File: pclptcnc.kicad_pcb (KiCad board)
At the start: 2 copper layers, 180.5 x 52.3 mm, 249 parts, among them P1 ARK825A-3, P3 ARK825A-4, P4 ARK825A-3, P5 ARK825A-3, P6 ARK825A-3, P7 ARK825A-3, P8 ARK825A-3, Q1 BC807-40, Q10 BC807-40, Q11 BC807-40, Q12 BC807-40, Q13 BC807-40, Q14 BC807-40, Q15 BC807-40, Q16 BC807-40, Q17 BC807-40, Q18 BC807-40, Q2 BC807-40, Q3 BC807-40, Q4 BC807-40, Q5 BC807-40, Q6 BC807-40, Q7 BC807-40, Q8 BC807-40, Q9 BC807-40, U1 74LVC1G3157GW, U10 SN74LVC2G17, U11 74HCT14, U12 SN74LVC2G17, U13 74HCT14, U2 HCPL2630, U3 HCPL2630, U4 HCPL2630, U5 HCPL2630, U6 HCPL2630, U7 HCPL2630, U8 74HCT14, U9 74HCT14, j1 DB25, j2 DB25

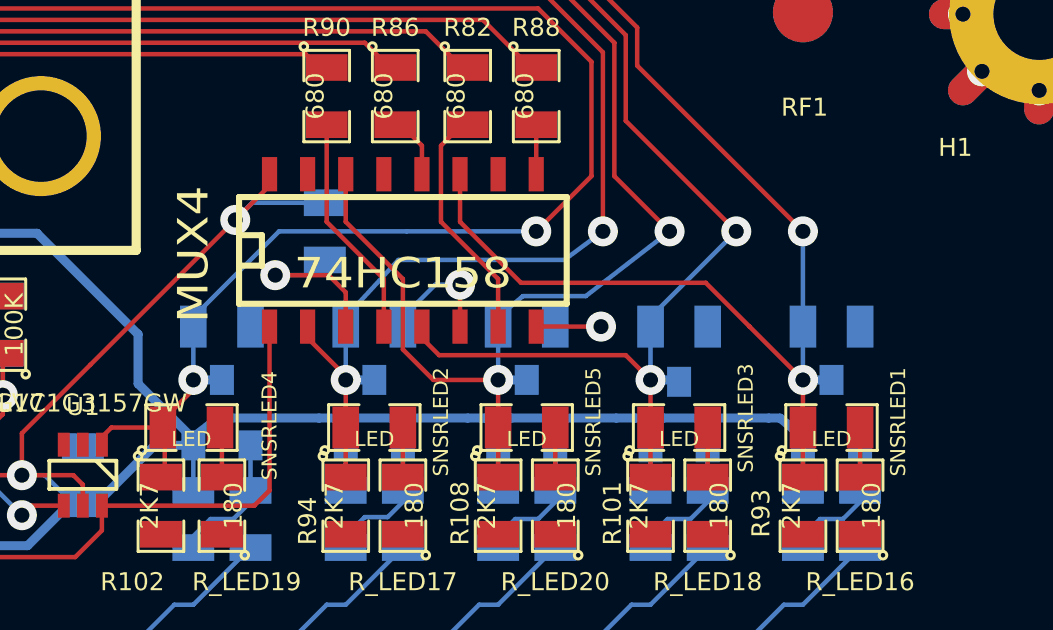
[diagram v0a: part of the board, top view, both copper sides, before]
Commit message: odd komponents removed
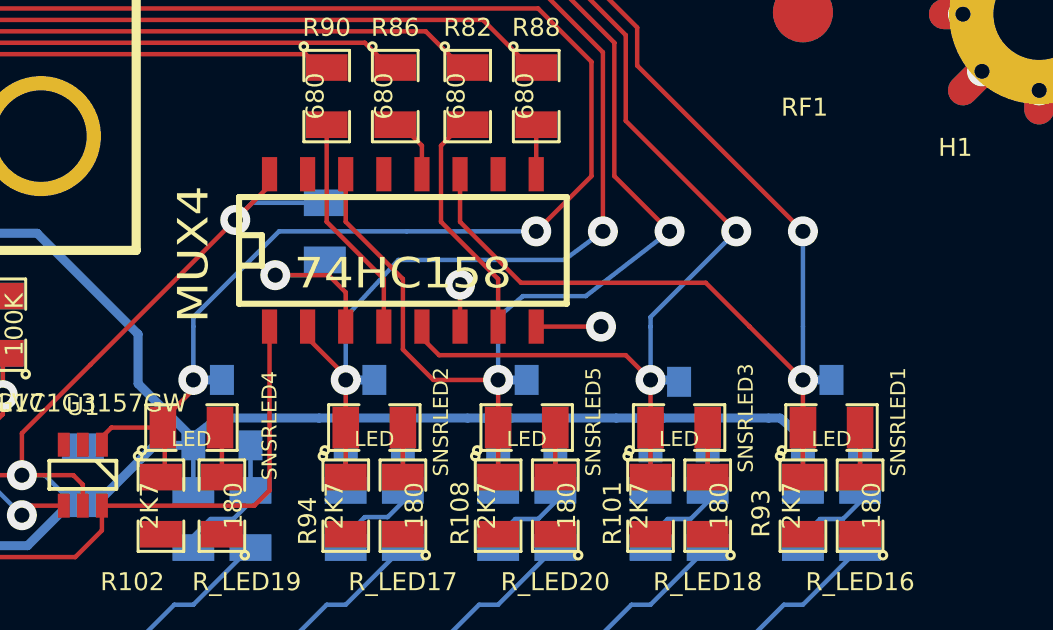
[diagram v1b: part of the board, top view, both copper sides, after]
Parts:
- removed R111, R112, R113, R114, R115: 100K, SM0805
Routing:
- net GND: track 391.3 -> 388.7 mm

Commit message: revision b
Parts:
- moved OPTOCPLR1 49.6 mm to (231.1, 108.6)
- moved OPTOCPLR5 49.6 mm to (220.9, 108.6)
- moved Q18 49.6 mm to (225.0, 92.1)
- moved R103 49.6 mm to (229.2, 95.6)
- moved R105 49.6 mm to (231.1, 95.6)
- moved R107 49.6 mm to (220.9, 111.2)
- moved R76 49.6 mm to (185.0, 117.5)
- moved R91 49.6 mm to (231.1, 111.2)
- moved R96 49.6 mm to (219.0, 95.6)
- moved R98 49.6 mm to (220.9, 95.6)
- moved SNSRLED5 49.6 mm to (225.0, 92.6)
- moved U12 49.6 mm to (206.2, 94.2)
- moved j2 49.6 mm to (185.4, 84.1)
- moved C5 49.6 mm to (95.7, 87.6)
- moved MUX4 49.6 mm to (220.9, 86.7)
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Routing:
- net /ISOLATED_GND: track 24.8 -> 55.5 mm, vias 1 -> 2
- net GND: track 388.7 -> 398.3 mm
- net /VCC_NFused: track 0.00 -> 3.41 mm
- net /ISOLATED_VCC: track 626.3 -> 629.4 mm
- net (no net): vias 1 -> 0
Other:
- board text added: "GND"
- board text added: "VCC"
- board text added: "VIN"

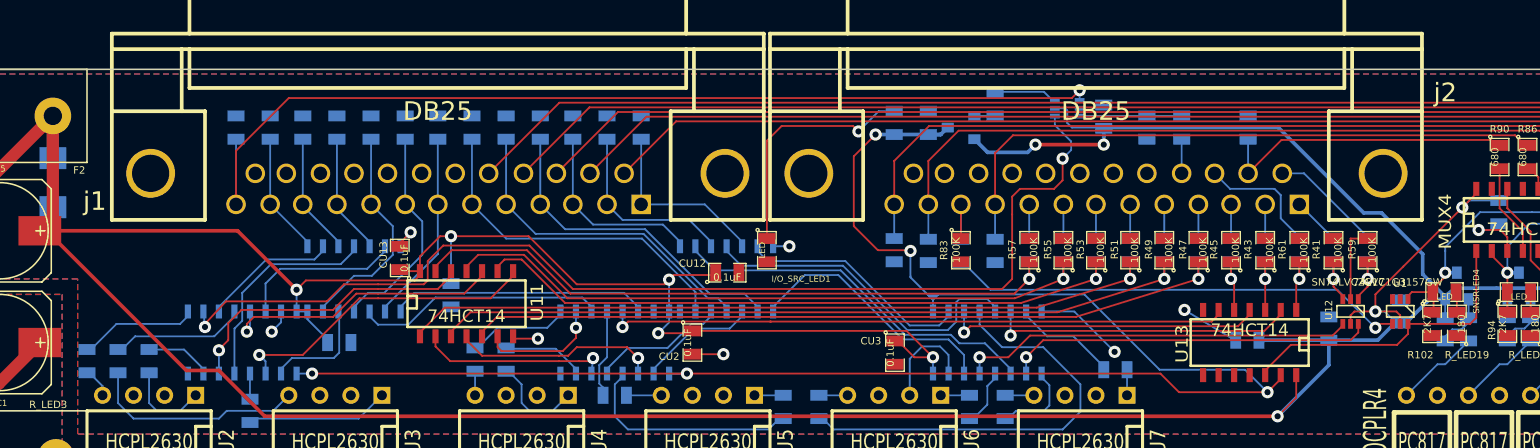
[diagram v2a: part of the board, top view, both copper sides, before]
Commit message: starting work on adding emergency stop switch selection
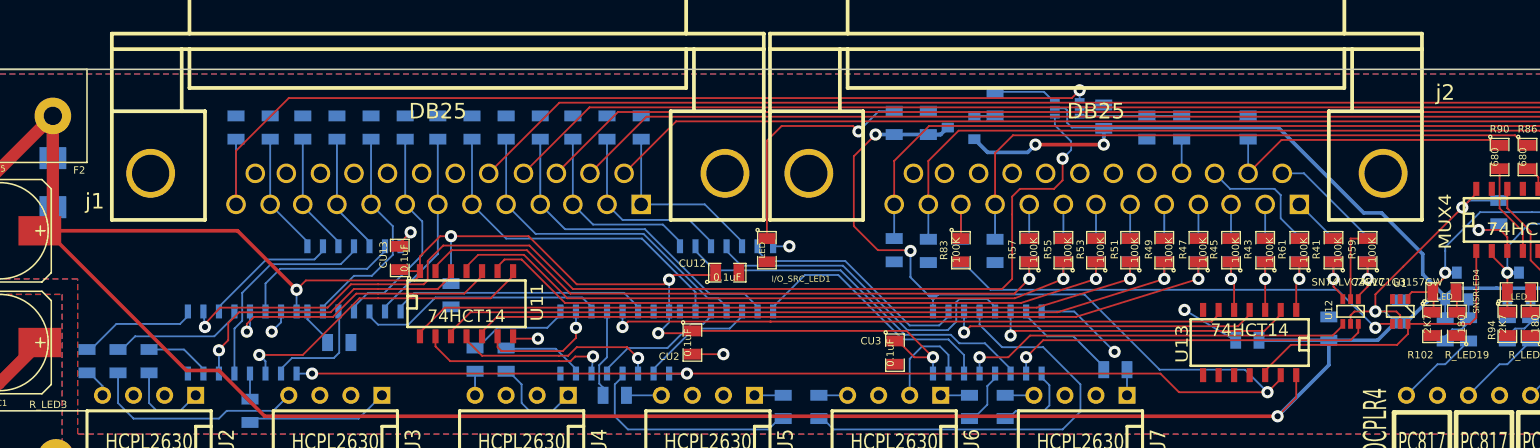
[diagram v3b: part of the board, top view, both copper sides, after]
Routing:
- net /PC6: track 15.6 -> 16.1 mm
